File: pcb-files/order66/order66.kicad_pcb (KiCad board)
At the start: 2 copper layers, 228.6 x 123 mm, 144 parts, among them J1 NICEVIEW, J2 Pouch Battery Connector, SW1 AUX1, SW10 Z, SW11 AUX7, SW12 2, SW13 W, SW14 S, SW15 X, SW16 LALT, SW17 3, SW18 E, SW19 D, SW2 ESC, SW20 C, SW21 GUI, SW22 4, SW23 R, SW24 F, SW25 V, SW26 RAISE, SW27 5, SW28 T, SW29 G, SW3 TAB, SW30 B, SW31 LSPACE, SW32 AUX2, SW33 6, SW34 Y, SW35 H, SW36 N, SW37 RSPACE, SW38 AUX3, SW39 7, SW4 CAPSLCK, SW40 U, SW41 J, SW42 M, SW43 LOWER, SW44 AUX4, SW45 8, SW46 I, SW47 K, SW48 ,<, SW49 LEFT, SW5 LSHIFT, SW50 9, SW51 O, SW52 L, SW53 .>, SW54 DOWN, SW55 AUX5, SW56 0, SW57 P, SW58 ;:, SW59 /?, SW6 LCTRL, SW60 UP, SW61 AUX6, SW62 BACKSPACE, SW63 BACKSLACH, SW64 ENTER, SW65 RSHIFT, SW66 RIGHT, SW67 RST, SW68 ON/OFF, SW7 1, SW8 Q, SW9 A, U1 NiceNano

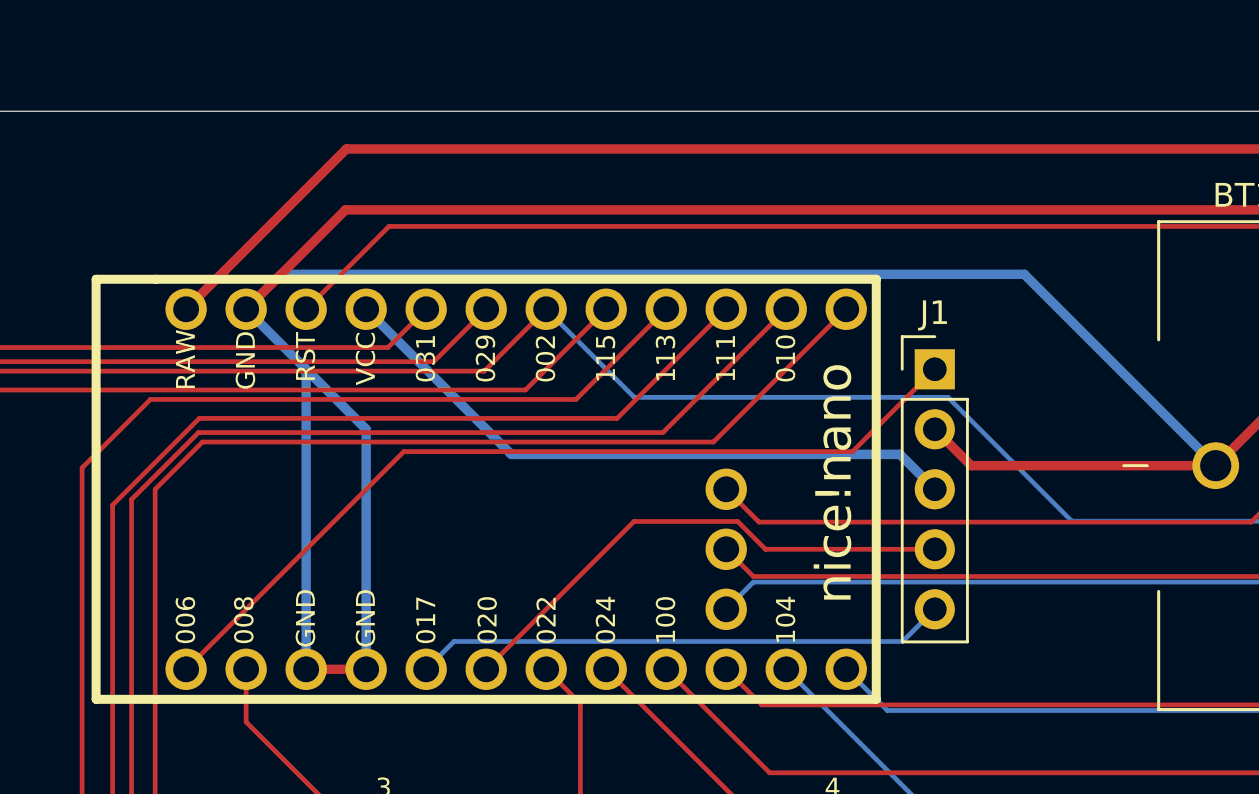
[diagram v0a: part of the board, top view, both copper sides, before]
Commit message: added support for millmax spring loaded swd pins for bootloader support
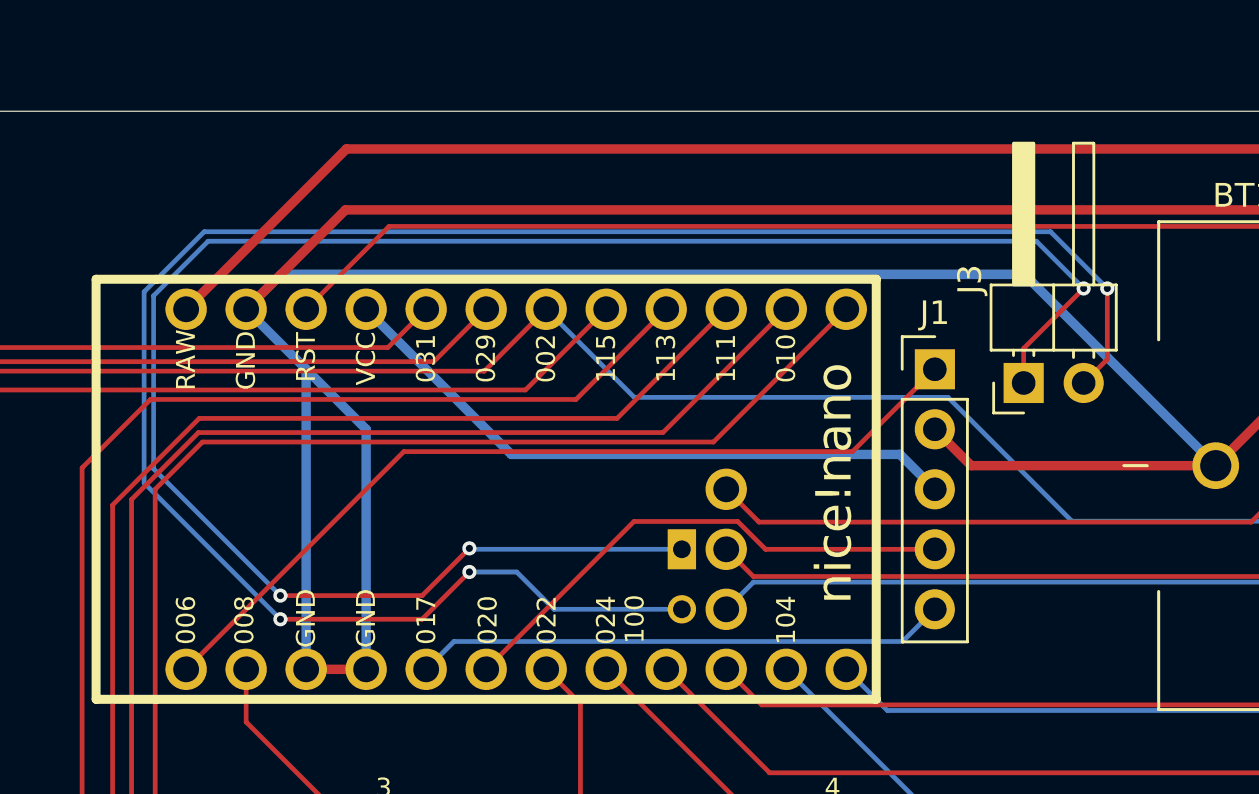
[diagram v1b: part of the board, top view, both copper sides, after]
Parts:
- added J3: swd connector, Connector_PinHeader_2.54mm:PinHeader_1x02_P2.54mm_Horizontal, F.Cu at (183.5, 75.0)
- added J6: millmax connector, Connector_PinHeader_2.54mm:PinHeader_1x02_P2.54mm_Vertical, F.Cu at (169.1, 82.0)
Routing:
- net SWD: track 0.00 -> 82.0 mm, vias 0 -> 3
- net SWC: track 0.00 -> 79.0 mm, vias 0 -> 3

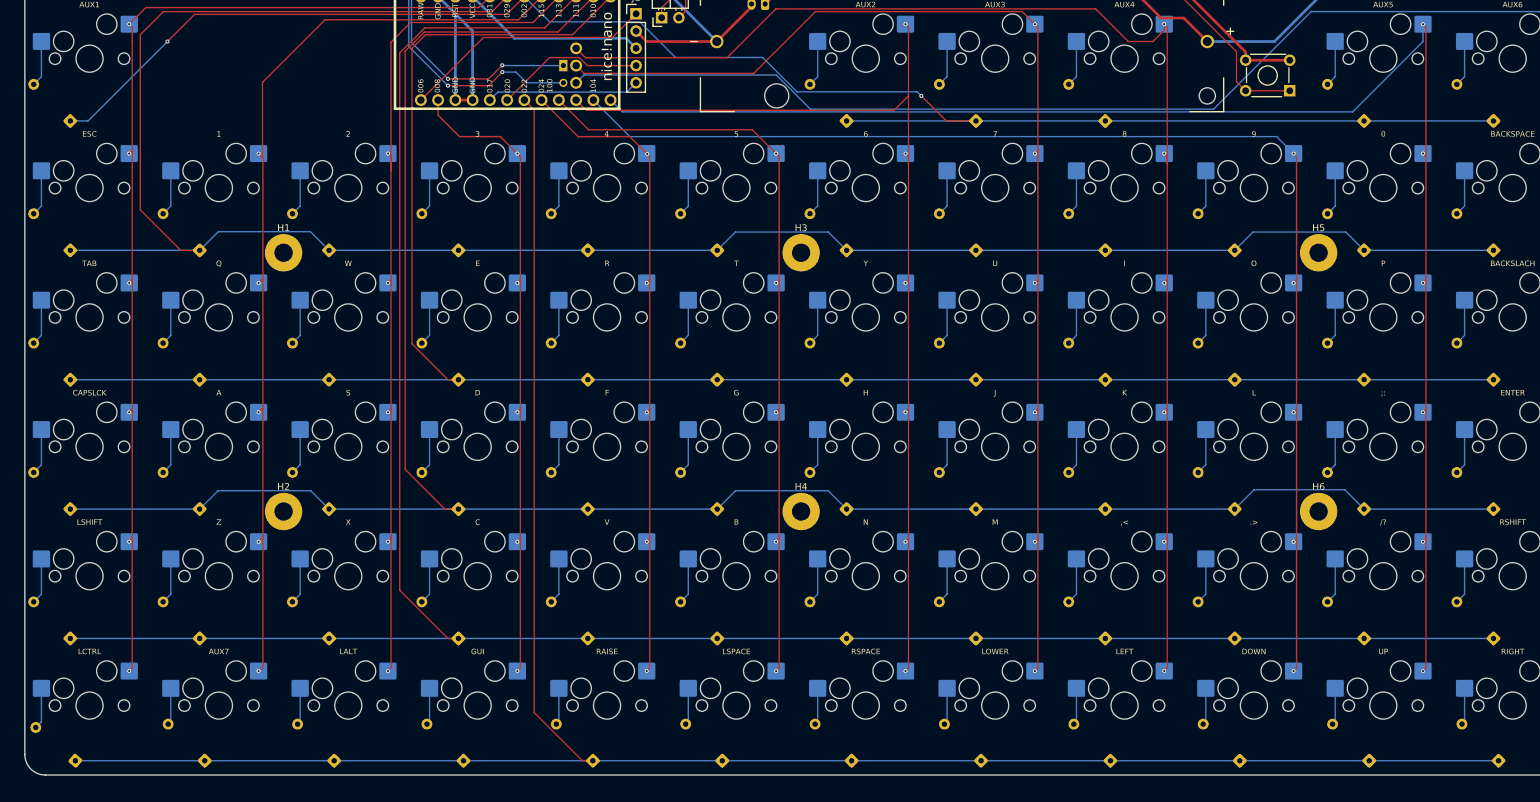
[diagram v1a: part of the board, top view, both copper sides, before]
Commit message: added the smd sod 123 package diode symbols. havent placed/routed all the footprints yet but seems to be okay. need to figure out what I want to do with the silkscreen references. probably should just place the base numbered one and dont use the other
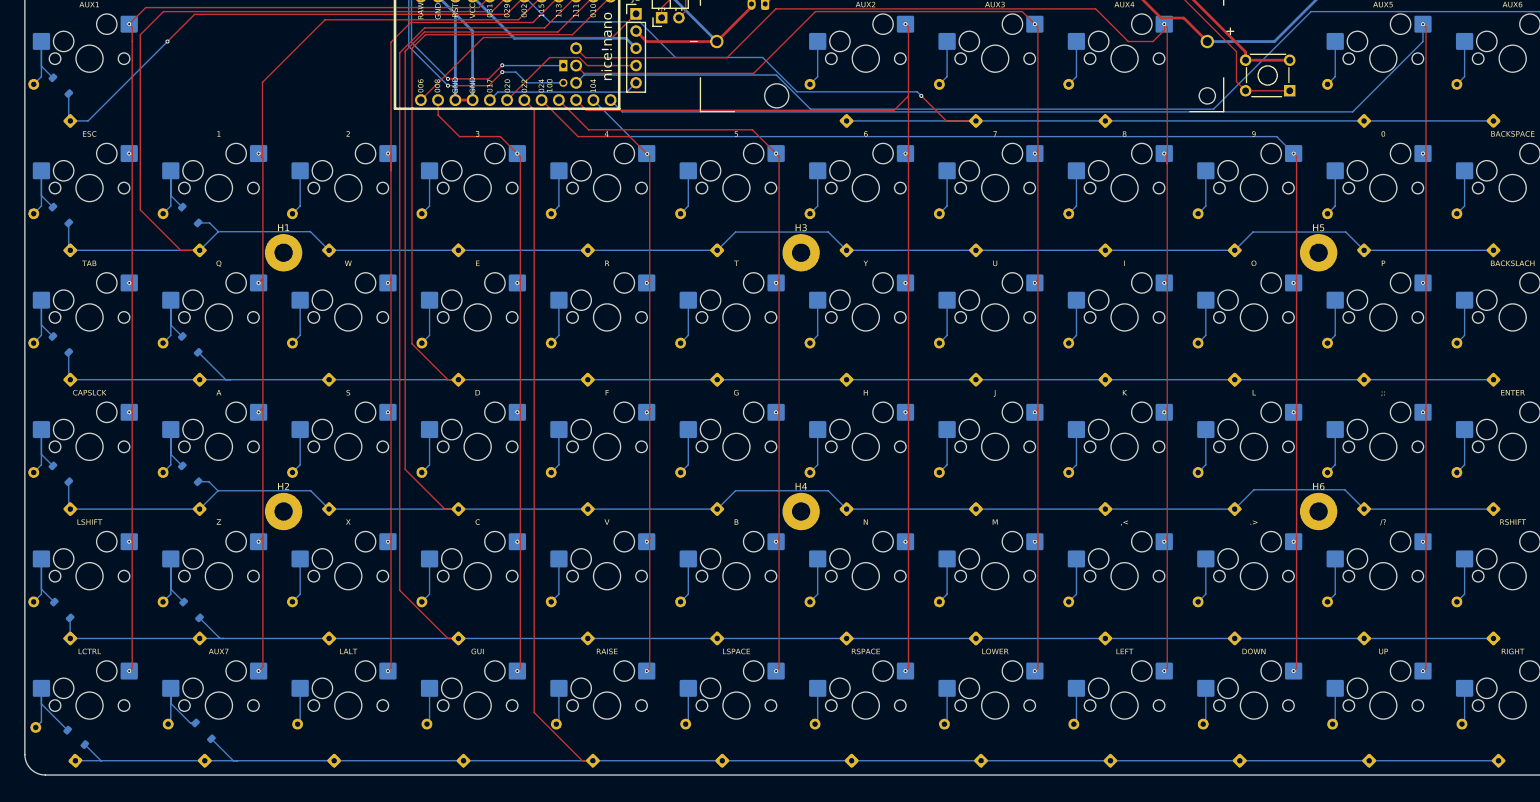
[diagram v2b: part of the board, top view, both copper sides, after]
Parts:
- added D101: 1N4148, Diode_SMD:D_SOD-123, B.Cu at (95.1, 85.0)
- added D102: 1N4148, Diode_SMD:D_SOD-123, B.Cu at (95.1, 104.0)
- added D103: 1N4148, Diode_SMD:D_SOD-123, B.Cu at (95.1, 123.1)
- added D104: 1N4148, Diode_SMD:D_SOD-123, B.Cu at (95.1, 142.2)
- added D105: 1N4148, Diode_SMD:D_SOD-123, B.Cu at (95.3, 162.2)
- added D106: 1N4148, Diode_SMD:D_SOD-123, B.Cu at (97.3, 181.0)
- added D107: 1N4148, Diode_SMD:D_SOD-123, B.Cu at (114.1, 104.0)
- added D108: 1N4148, Diode_SMD:D_SOD-123, B.Cu at (114.1, 123.1)
- added D109: 1N4148, Diode_SMD:D_SOD-123, B.Cu at (114.1, 142.2)
- added D110: 1N4148, Diode_SMD:D_SOD-123, B.Cu at (114.3, 162.2)
- added D111: 1N4148, Diode_SMD:D_SOD-123, B.Cu at (116.1, 180.0)
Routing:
- net ROW2: track 294.5 -> 305.1 mm
- net ROW5: track 311.9 -> 320.6 mm
- net ROW4: track 329.7 -> 337.6 mm
- net Net-(D106-A): track 6.11 -> 13.9 mm
- net ROW1: track 309.6 -> 317.3 mm
- net ROW3: track 319.2 -> 326.8 mm
- net Net-(D105-A): track 6.79 -> 13.9 mm
- net Net-(D10-A): track 6.79 -> 13.9 mm
- net Net-(D11-A): track 5.43 -> 12.5 mm
- net Net-(D109-A): track 6.79 -> 12.8 mm
- net Net-(D103-A): track 6.79 -> 12.8 mm
- net Net-(D1-A): track 6.79 -> 12.8 mm
- net Net-(D108-A): track 6.79 -> 12.8 mm
- net Net-(D107-A): track 6.79 -> 12.8 mm
- net Net-(D104-A): track 6.79 -> 12.8 mm
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
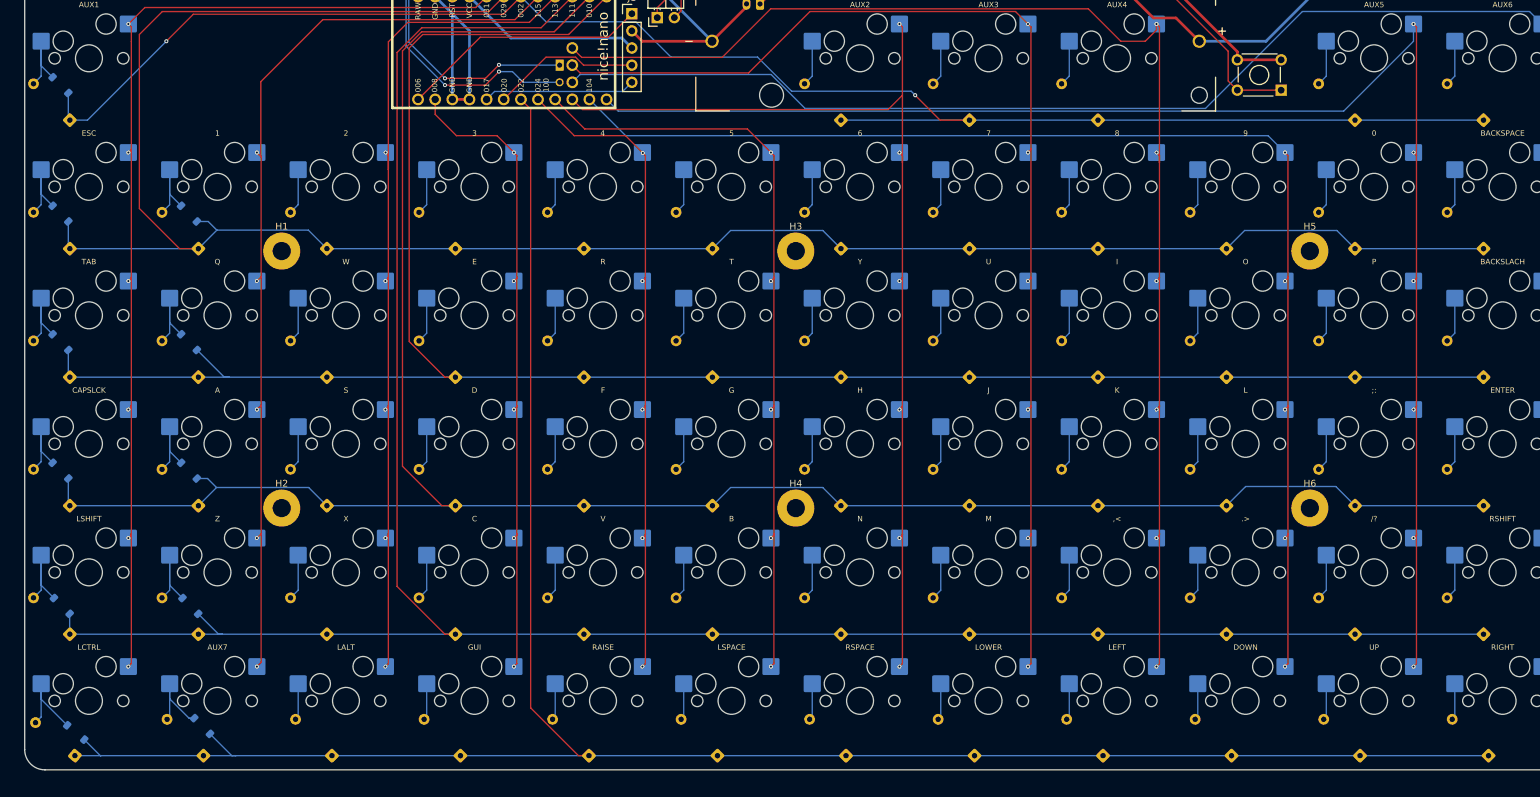
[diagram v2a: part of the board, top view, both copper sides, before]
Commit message: placed all diode footprints. need to sort out the silkscreen overlaps
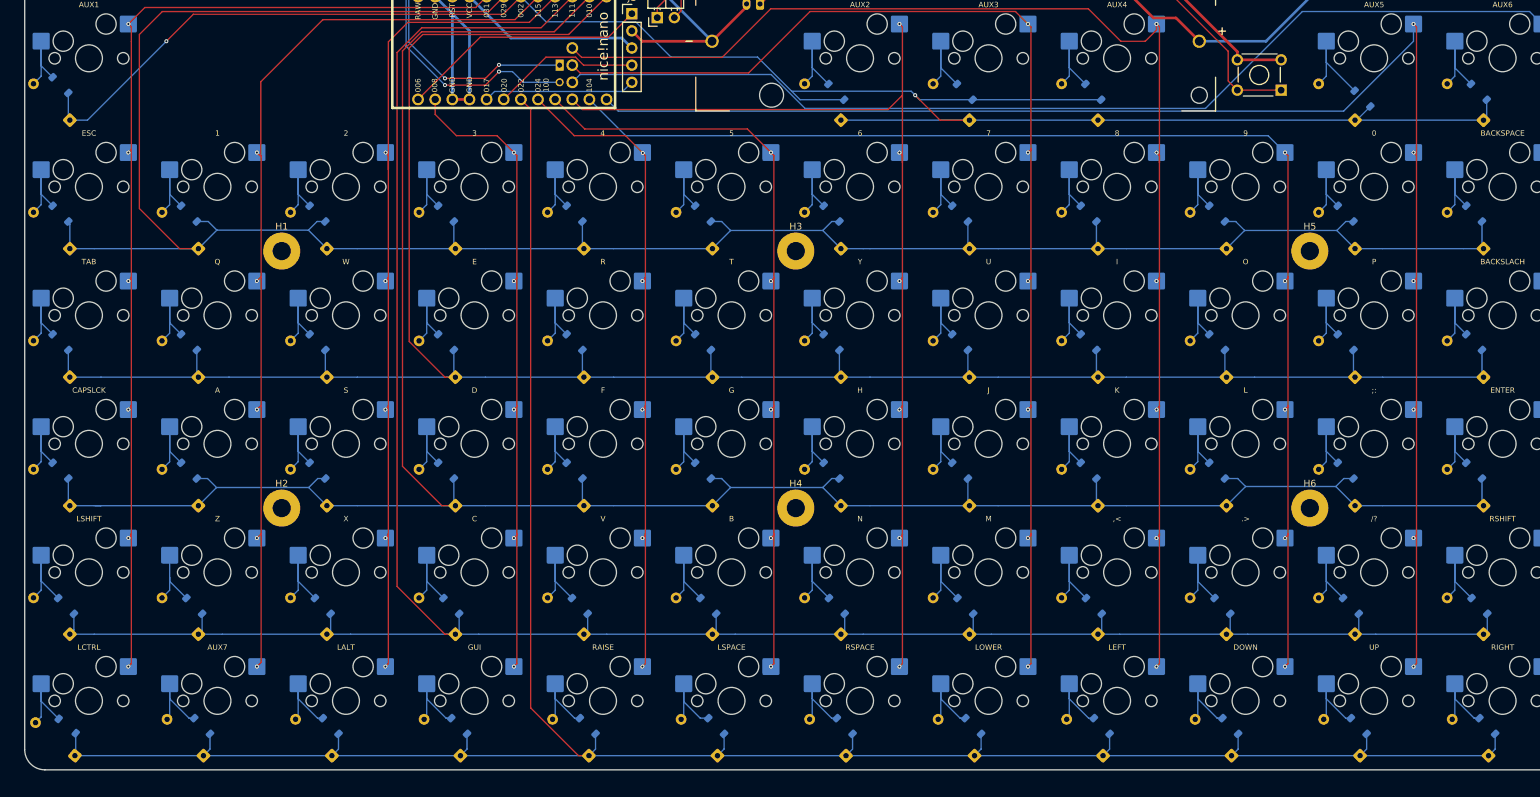
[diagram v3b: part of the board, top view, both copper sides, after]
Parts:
- added D112: 1N4148, Diode_SMD:D_SOD-123, B.Cu at (133.2, 104.0)
- added D113: 1N4148, Diode_SMD:D_SOD-123, B.Cu at (133.2, 123.1)
- added D114: 1N4148, Diode_SMD:D_SOD-123, B.Cu at (133.2, 142.2)
- added D115: 1N4148, Diode_SMD:D_SOD-123, B.Cu at (133.9, 162.2)
- added D116: 1N4148, Diode_SMD:D_SOD-123, B.Cu at (135.1, 180.0)
- added D117: 1N4148, Diode_SMD:D_SOD-123, B.Cu at (152.2, 104.0)
- added D118: 1N4148, Diode_SMD:D_SOD-123, B.Cu at (152.2, 123.1)
- added D119: 1N4148, Diode_SMD:D_SOD-123, B.Cu at (152.2, 142.2)
- added D120: 1N4148, Diode_SMD:D_SOD-123, B.Cu at (153.0, 162.2)
- added D121: 1N4148, Diode_SMD:D_SOD-123, B.Cu at (154.2, 180.0)
- added D122: 1N4148, Diode_SMD:D_SOD-123, B.Cu at (171.3, 104.0)
- added D123: 1N4148, Diode_SMD:D_SOD-123, B.Cu at (171.3, 123.1)
- added D124: 1N4148, Diode_SMD:D_SOD-123, B.Cu at (171.3, 142.2)
- added D125: 1N4148, Diode_SMD:D_SOD-123, B.Cu at (172.0, 162.2)
- added D126: 1N4148, Diode_SMD:D_SOD-123, B.Cu at (173.2, 180.0)
- added D127: 1N4148, Diode_SMD:D_SOD-123, B.Cu at (190.3, 104.0)
- added D128: 1N4148, Diode_SMD:D_SOD-123, B.Cu at (190.3, 123.1)
- added D129: 1N4148, Diode_SMD:D_SOD-123, B.Cu at (190.3, 142.2)
- added D130: 1N4148, Diode_SMD:D_SOD-123, B.Cu at (191.1, 162.2)
- added D131: 1N4148, Diode_SMD:D_SOD-123, B.Cu at (192.3, 180.0)
- added D132: 1N4148, Diode_SMD:D_SOD-123, B.Cu at (210.1, 86.0)
- added D133: 1N4148, Diode_SMD:D_SOD-123, B.Cu at (209.4, 104.0)
- added D134: 1N4148, Diode_SMD:D_SOD-123, B.Cu at (209.4, 123.1)
- added D135: 1N4148, Diode_SMD:D_SOD-123, B.Cu at (209.4, 142.2)
- added D136: 1N4148, Diode_SMD:D_SOD-123, B.Cu at (210.1, 162.2)
- added D137: 1N4148, Diode_SMD:D_SOD-123, B.Cu at (211.3, 180.0)
- added D138: 1N4148, Diode_SMD:D_SOD-123, B.Cu at (229.1, 86.0)
- added D139: 1N4148, Diode_SMD:D_SOD-123, B.Cu at (228.4, 104.0)
- added D140: 1N4148, Diode_SMD:D_SOD-123, B.Cu at (228.4, 123.1)
- added D141: 1N4148, Diode_SMD:D_SOD-123, B.Cu at (228.4, 142.2)
- added D142: 1N4148, Diode_SMD:D_SOD-123, B.Cu at (229.2, 162.2)
- added D143: 1N4148, Diode_SMD:D_SOD-123, B.Cu at (230.4, 180.0)
- added D144: 1N4148, Diode_SMD:D_SOD-123, B.Cu at (248.2, 86.0)
- added D145: 1N4148, Diode_SMD:D_SOD-123, B.Cu at (247.5, 104.0)
- added D146: 1N4148, Diode_SMD:D_SOD-123, B.Cu at (247.5, 123.1)
- added D147: 1N4148, Diode_SMD:D_SOD-123, B.Cu at (247.5, 142.2)
- added D148: 1N4148, Diode_SMD:D_SOD-123, B.Cu at (248.2, 162.2)
- added D149: 1N4148, Diode_SMD:D_SOD-123, B.Cu at (249.4, 180.0)
- added D150: 1N4148, Diode_SMD:D_SOD-123, B.Cu at (266.5, 104.0)
- added D151: 1N4148, Diode_SMD:D_SOD-123, B.Cu at (266.5, 123.1)
- added D152: 1N4148, Diode_SMD:D_SOD-123, B.Cu at (266.5, 142.2)
- added D153: 1N4148, Diode_SMD:D_SOD-123, B.Cu at (267.3, 162.2)
- added D154: 1N4148, Diode_SMD:D_SOD-123, B.Cu at (268.5, 180.0)
- added D155: 1N4148, Diode_SMD:D_SOD-123, B.Cu at (288.1, 87.0)
- added D156: 1N4148, Diode_SMD:D_SOD-123, B.Cu at (285.6, 104.0)
- added D157: 1N4148, Diode_SMD:D_SOD-123, B.Cu at (285.6, 123.1)
- added D158: 1N4148, Diode_SMD:D_SOD-123, B.Cu at (285.6, 142.2)
- added D159: 1N4148, Diode_SMD:D_SOD-123, B.Cu at (286.3, 162.2)
- added D160: 1N4148, Diode_SMD:D_SOD-123, B.Cu at (287.5, 180.0)
- added D161: 1N4148, Diode_SMD:D_SOD-123, B.Cu at (305.3, 86.0)
- added D162: 1N4148, Diode_SMD:D_SOD-123, B.Cu at (304.6, 104.0)
- added D163: 1N4148, Diode_SMD:D_SOD-123, B.Cu at (304.6, 123.1)
- added D164: 1N4148, Diode_SMD:D_SOD-123, B.Cu at (304.6, 142.2)
- added D165: 1N4148, Diode_SMD:D_SOD-123, B.Cu at (305.4, 162.2)
- added D166: 1N4148, Diode_SMD:D_SOD-123, B.Cu at (306.6, 180.0)
- moved D106 1.59 mm to (96.1, 180.0)
- moved D105 0.63 mm to (95.9, 162.2)
- moved D110 0.58 mm to (114.9, 162.2)
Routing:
- net ROW0: track 248.1 -> 290.6 mm
- net ROW2: track 305.1 -> 344.0 mm
- net ROW3: track 326.8 -> 364.4 mm
- net ROW1: track 317.3 -> 354.2 mm
- net ROW5: track 320.6 -> 355.3 mm
- net ROW4: track 337.6 -> 369.3 mm
- net Net-(D155-A): track 6.79 -> 15.9 mm
- net Net-(D159-A): track 6.79 -> 14.2 mm
- net Net-(D153-A): track 6.79 -> 14.2 mm
- net Net-(D148-A): track 6.79 -> 14.2 mm
- net Net-(D136-A): track 6.79 -> 14.2 mm
- net Net-(D130-A): track 6.79 -> 14.2 mm
- net Net-(D125-A): track 6.79 -> 14.2 mm
- net Net-(D120-A): track 6.79 -> 14.2 mm
- net Net-(D165-A): track 6.79 -> 14.2 mm
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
